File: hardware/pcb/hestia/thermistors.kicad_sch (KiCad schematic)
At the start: 60 parts, among them J10 Conn_01x02_Female, J11 Conn_01x02_Female, J12 Conn_01x02_Female, J13 Conn_01x02_Female, J14 Conn_01x02_Female, J15 Conn_01x02_Female, J16 Conn_01x02_Female, J7 Conn_01x02_Female, J8 Conn_01x02_Female, J9 Conn_01x02_Female, U4 MAX31725MTA+T, U5 MAX31725MTA+T, U6 MAX31725MTA+T, U7 MAX31725MTA+T

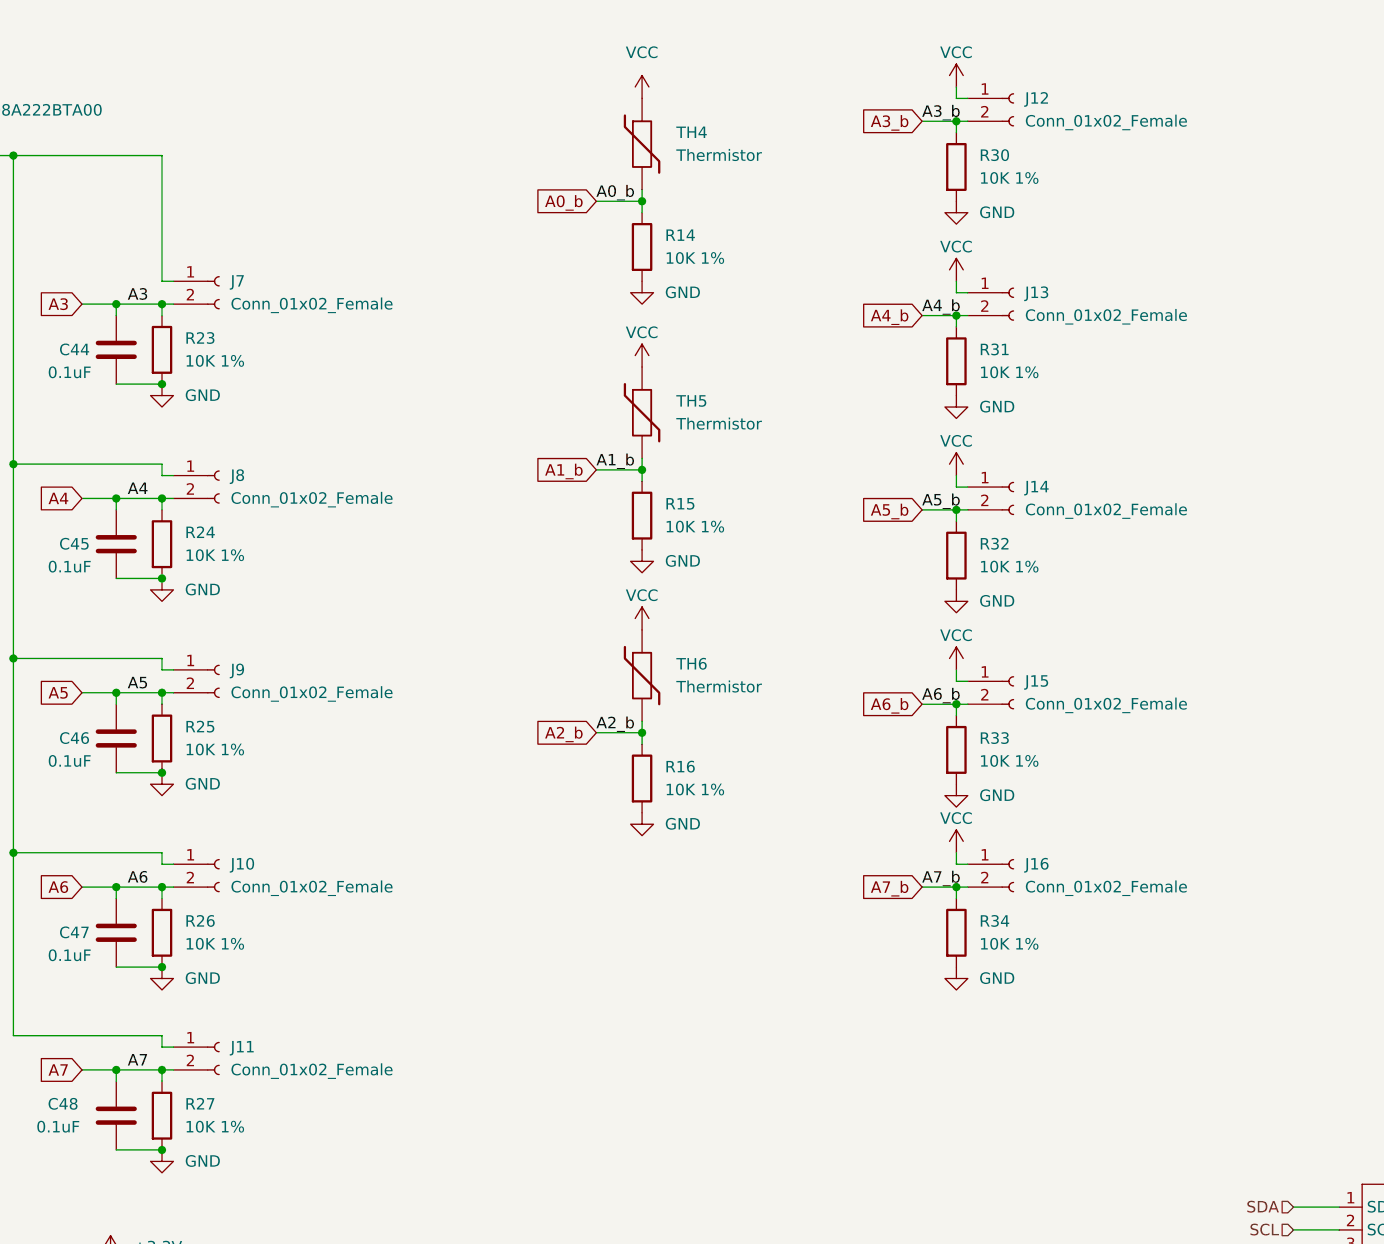
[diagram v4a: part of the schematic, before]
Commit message: don't update pcb from schematic yet. added and changed footprint info on schematic for 1.5mm pitch term pads, crystals, jtag vcc jumper. a bunch of components are out of sync with the pcb, the schematic is unaware that the components are already on the PCB. some components from the first versions were not in the hestia parts library - hopefully this commit adds them back? was a commit made without a pull?
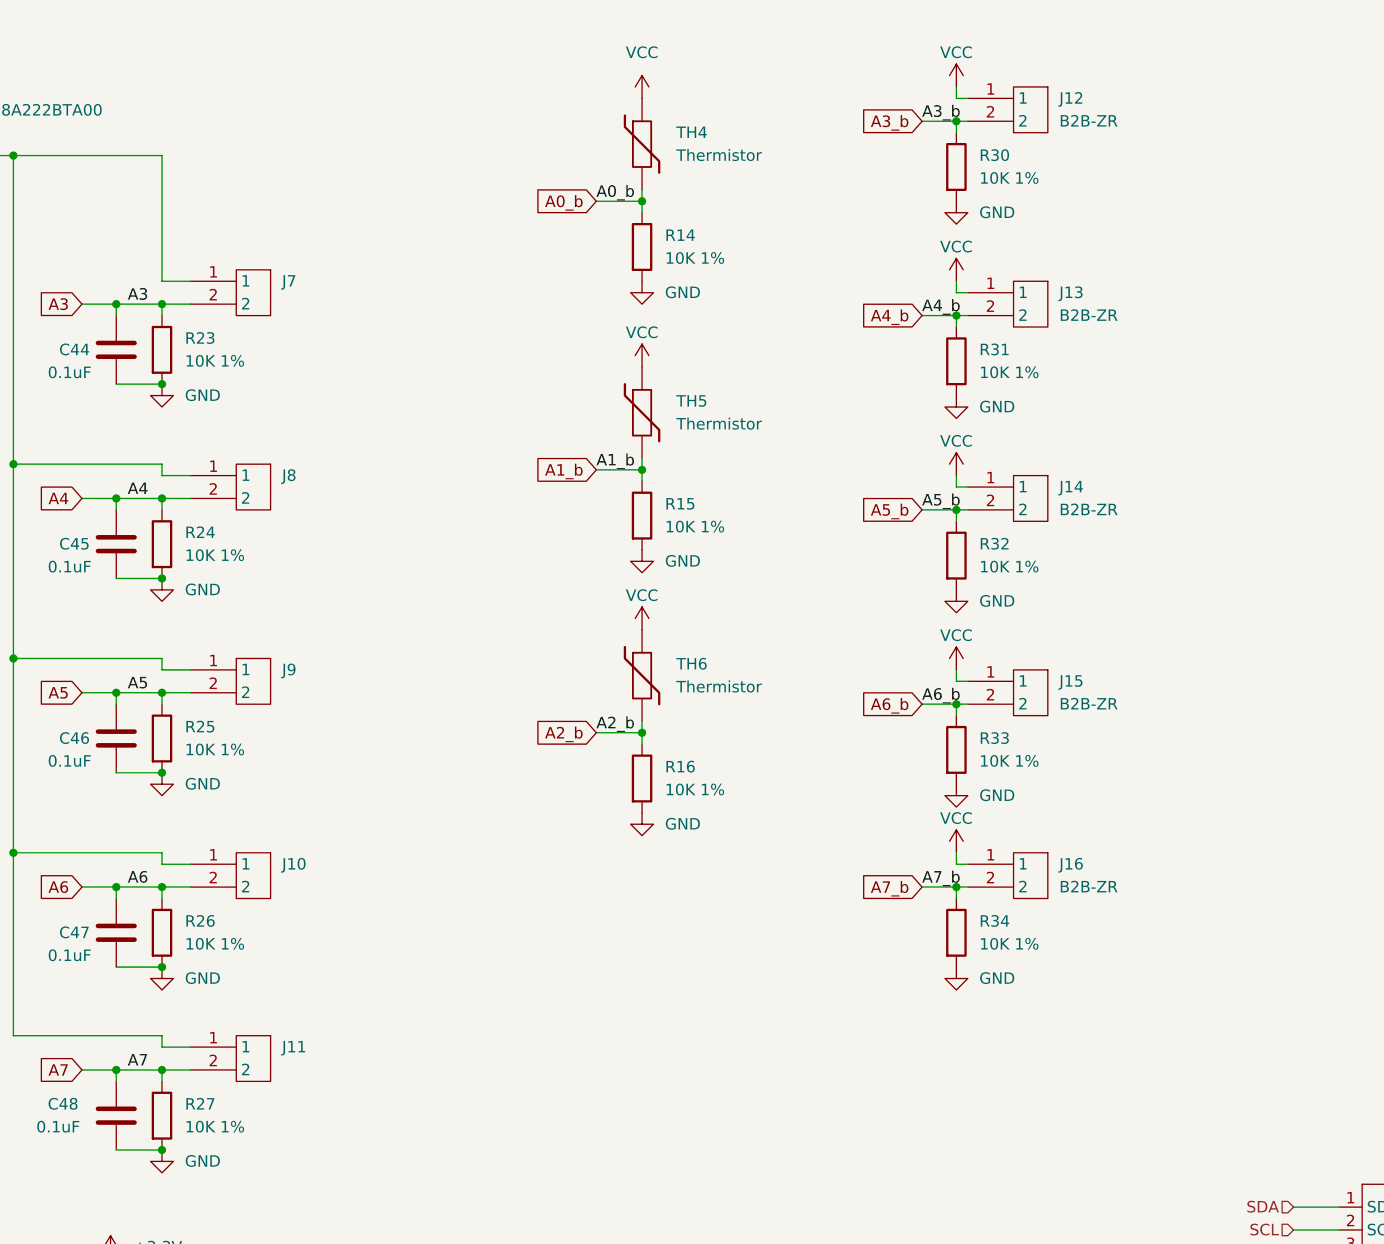
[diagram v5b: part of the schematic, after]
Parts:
- removed J10, J11, J12, J13, J14, J15, J16, J7, J8, J9: Conn_01x02_Female, Connector_PinHeader_1.27mm:PinHeader_1x02_P1.27mm_Vertical, symbol Connector:Conn_01x02_Female
- added J10, J11, J7, J8, J9: (no value), symbol Hestia:B2B-ZR
- added J12, J13, J14, J15, J16: B2B-ZR, Hestia:B2B-ZR(LF)(SN), symbol Hestia:B2B-ZR
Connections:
- net A3: now also J7.2
- net A3_b: now also J12.2
- net A4: now also J8.2
- net A4_b: now also J13.2
- net A5: now also J9.2
- net A5_b: now also J14.2
- net A6: now also J10.2
- net A6_b: now also J15.2
- net A7: now also J11.2
- net A7_b: now also J16.2
- net VCC: now also J12.1, J13.1, J14.1, J15.1, J16.1
- net at C50.1, FB4.1: now also J10.1, J11.1, J7.1, J8.1, J9.1

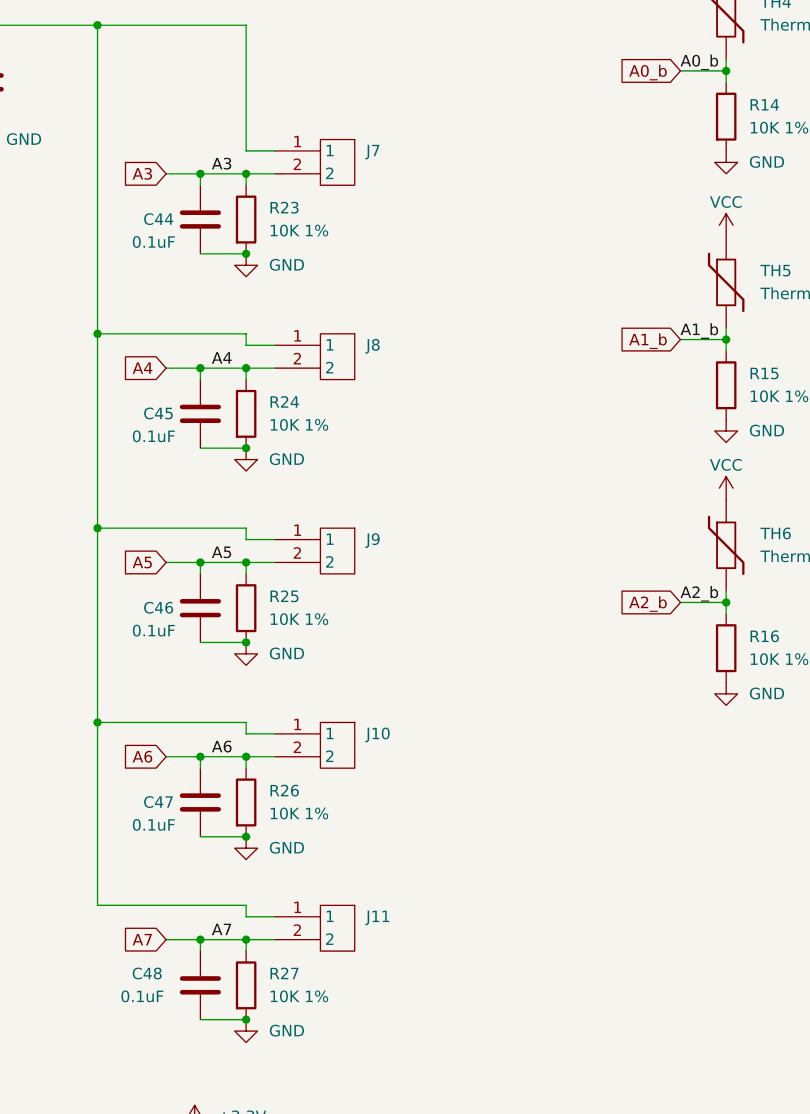
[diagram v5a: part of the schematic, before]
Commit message: Sorted out checmatic <=> pcb update sync. Changed JTAG pinheader to shrouded IDC connector footprint. temp place 2 pin 1.5mm pitch pin sockets. remove i2c voltage translator transistors, changed to i2c buffer ic. Added schematic symbol for cubesat board mount rods and linked to the hole footprint. TODO:rearrange components and traces, move J1&J2 by 3mm, wire restraint holes for wired thermistors, heater current measurement components, resettable fuses, bimetal switch footprint/pads, check I2C addresses
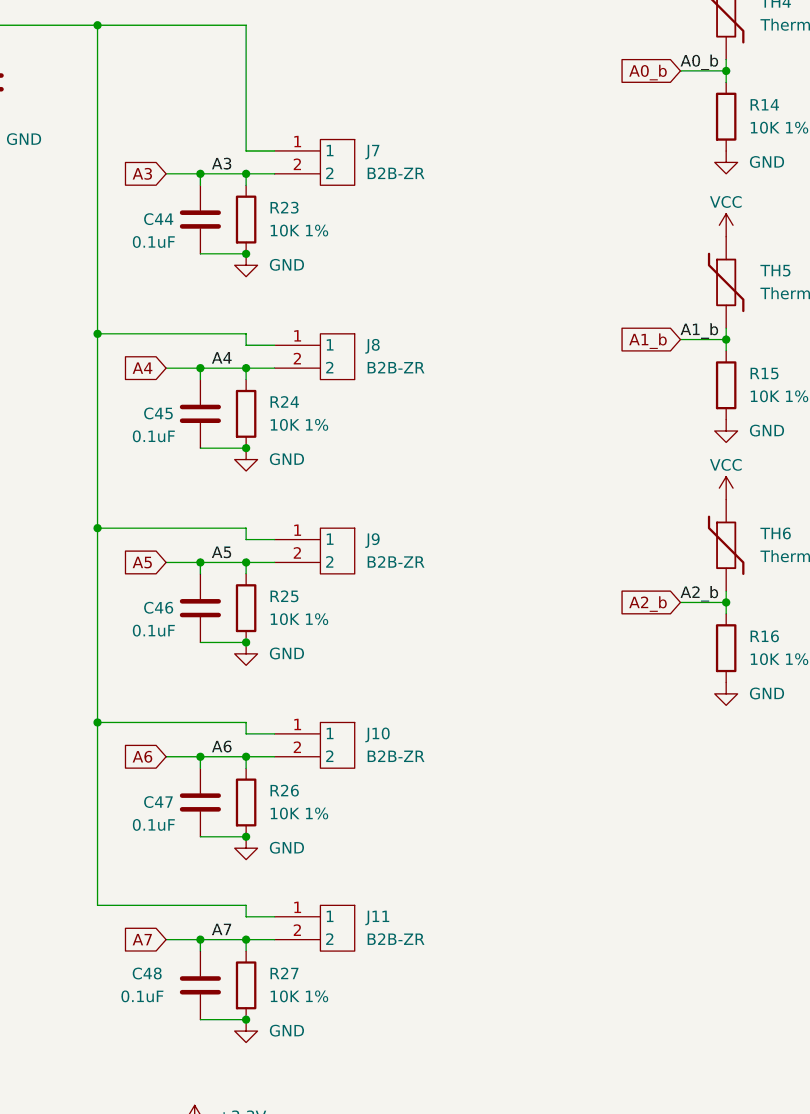
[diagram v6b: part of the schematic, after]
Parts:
- J10, J11, J7, J8, J9: value (none) -> B2B-ZR; footprint (none) -> Hestia:B2B-ZR(LF)(SN)
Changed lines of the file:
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@@
       (effects (font (size 1.27 1.27)) (justify right))
     )
-    (property "Value" "" (id 1) (at 109.22 67.3099 0)
-      (effects (font (size 1.27 1.27)) (justify right))
-    )
-    (property "Footprint" "" (id 2) (at 104.14 64.77 0)
+    (property "Value" "B2B-ZR" (id 1) (at 109.22 67.3099 0)
+      (effects (font (size 1.27 1.27)) (justify right))
+    )
+    (property "Footprint" "Hestia:B2B-ZR(LF)(SN)" (id 2) (at 104.14 64.77 0)
       (effects (font (size 1.27 1.27)) hide)
     )
@@
       (effects (font (size 1.27 1.27)) (justify right))
     )
-    (property "Value" "" (id 1) (at 109.22 45.7199 0)
-      (effects (font (size 1.27 1.27)) (justify right))
-    )
-    (property "Footprint" "" (id 2) (at 104.14 43.18 0)
+    (property "Value" "B2B-ZR" (id 1) (at 109.22 45.7199 0)
+      (effects (font (size 1.27 1.27)) (justify right))
+    )
+    (property "Footprint" "Hestia:B2B-ZR(LF)(SN)" (id 2) (at 104.14 43.18 0)
       (effects (font (size 1.27 1.27)) hide)
     )
@@
       (effects (font (size 1.27 1.27)) (justify right))
     )
-    (property "Value" "" (id 1) (at 109.22 88.8999 0)
-      (effects (font (size 1.27 1.27)) (justify right))
-    )
-    (property "Footprint" "" (id 2) (at 104.14 86.36 0)
+    (property "Value" "B2B-ZR" (id 1) (at 109.22 88.8999 0)
+      (effects (font (size 1.27 1.27)) (justify right))
+    )
+    (property "Footprint" "Hestia:B2B-ZR(LF)(SN)" (id 2) (at 104.14 86.36 0)
       (effects (font (size 1.27 1.27)) hide)
     )
@@
       (effects (font (size 1.27 1.27)) (justify right))
     )
-    (property "Value" "" (id 1) (at 109.22 110.4899 0)
-      (effects (font (size 1.27 1.27)) (justify right))
-    )
-    (property "Footprint" "" (id 2) (at 104.14 107.95 0)
+    (property "Value" "B2B-ZR" (id 1) (at 109.22 110.4899 0)
+      (effects (font (size 1.27 1.27)) (justify right))
+    )
+    (property "Footprint" "Hestia:B2B-ZR(LF)(SN)" (id 2) (at 104.14 107.95 0)
       (effects (font (size 1.27 1.27)) hide)
     )
@@
       (effects (font (size 1.27 1.27)) (justify right))
     )
-    (property "Value" "" (id 1) (at 109.22 130.8099 0)
-      (effects (font (size 1.27 1.27)) (justify right))
-    )
-    (property "Footprint" "" (id 2) (at 104.14 128.27 0)
-      (effects (font (size 1.27 1.27)) hide)
-    )
+    (property "Value" "B2B-ZR" (id 1) (at 109.22 130.8099 0)
+      (effects (font (size 1.27 1.27)) (justify right))
+    )
+    (property "Footprint" "Hestia:B2B-ZR(LF)(SN)" (id 2) (at 104.14 128.27 0)
+      (effects (font (size 1.27 1.27)) hide)
+    )

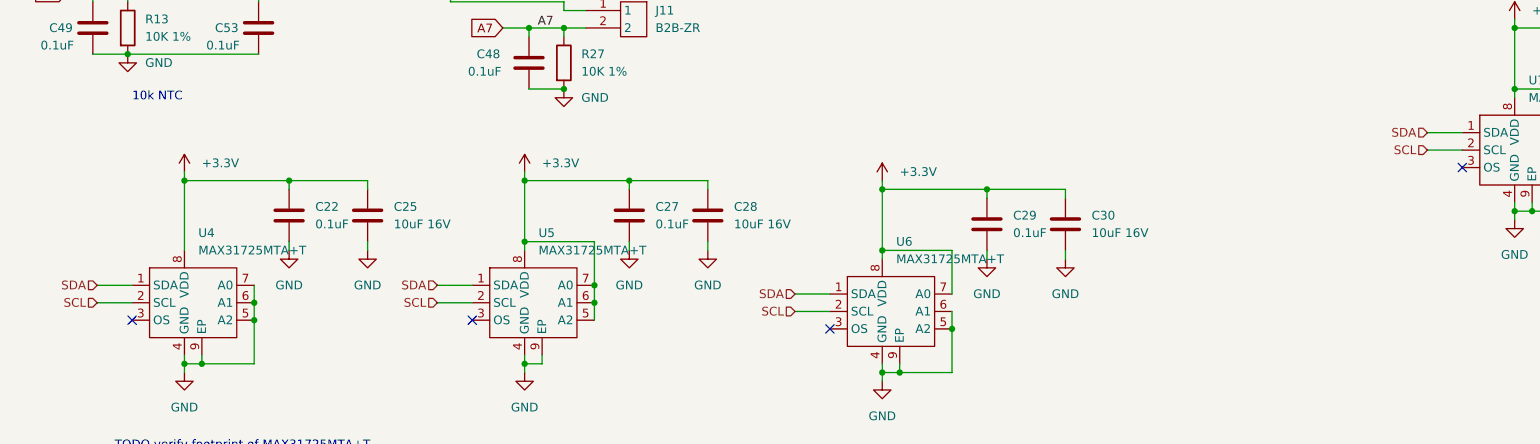
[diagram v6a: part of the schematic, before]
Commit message: more PCB trace changes on jtag, picolock connectors, i2c translator and I2C SDA,SCL, LEDs, Reset Switch
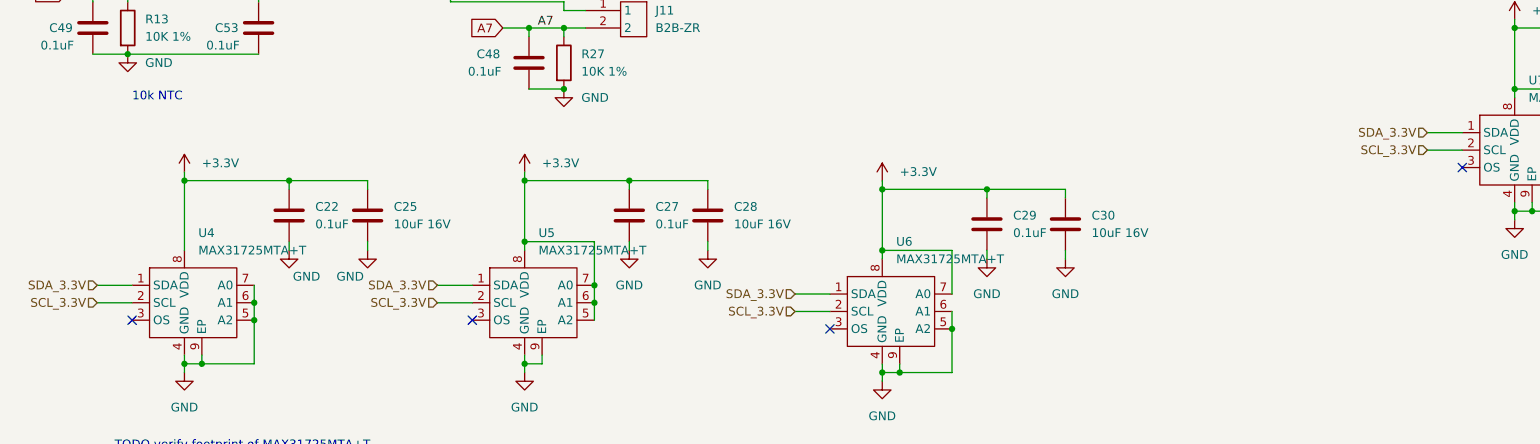
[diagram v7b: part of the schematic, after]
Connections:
- net SCL renamed SCL_3.3V
- net SDA renamed SDA_3.3V
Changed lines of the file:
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@@
     )
   )
-  (hierarchical_label "SDA" (shape input) (at 27.94 168.275 180)
-    (effects (font (size 1.27 1.27)) (justify right))
-  )
-  (hierarchical_label "SCL" (shape input) (at 221.615 148.59 180)
-    (effects (font (size 1.27 1.27)) (justify right))
-  )
-  (hierarchical_label "SDA" (shape input) (at 77.47 168.275 180)
-    (effects (font (size 1.27 1.27)) (justify right))
-  )
-  (hierarchical_label "SCL" (shape input) (at 27.94 170.815 180)
-    (effects (font (size 1.27 1.27)) (justify right))
-  )
-  (hierarchical_label "SCL" (shape input) (at 77.47 170.815 180)
-    (effects (font (size 1.27 1.27)) (justify right))
-  )
-  (hierarchical_label "SCL" (shape input) (at 129.54 172.085 180)
-    (effects (font (size 1.27 1.27)) (justify right))
-  )
-  (hierarchical_label "SDA" (shape input) (at 129.54 169.545 180)
-    (effects (font (size 1.27 1.27)) (justify right))
-  )
-  (hierarchical_label "SDA" (shape input) (at 221.615 146.05 180)
+  (hierarchical_label "SDA_3.3V" (shape input) (at 27.94 168.275 180)
+    (effects (font (size 1.27 1.27)) (justify right))
+  )
+  (hierarchical_label "SCL_3.3V" (shape input) (at 221.615 148.59 180)
+    (effects (font (size 1.27 1.27)) (justify right))
+  )
+  (hierarchical_label "SDA_3.3V" (shape input) (at 77.47 168.275 180)
+    (effects (font (size 1.27 1.27)) (justify right))
+  )
+  (hierarchical_label "SCL_3.3V" (shape input) (at 27.94 170.815 180)
+    (effects (font (size 1.27 1.27)) (justify right))
+  )
+  (hierarchical_label "SCL_3.3V" (shape input) (at 77.47 170.815 180)
+    (effects (font (size 1.27 1.27)) (justify right))
+  )
+  (hierarchical_label "SCL_3.3V" (shape input) (at 129.54 172.085 180)
+    (effects (font (size 1.27 1.27)) (justify right))
+  )
+  (hierarchical_label "SDA_3.3V" (shape input) (at 129.54 169.545 180)
+    (effects (font (size 1.27 1.27)) (justify right))
+  )
+  (hierarchical_label "SDA_3.3V" (shape input) (at 221.615 146.05 180)
     (effects (font (size 1.27 1.27)) (justify right))
   )
@@
   )
   (symbol (lib_id "power:GND") (at 67.31 163.195 0) (unit 1)
-    (in_bom yes) (on_board yes) (fields_autoplaced)
+    (in_bom yes) (on_board yes)
     (property "Reference" "#PWR0153" (id 0) (at 67.31 169.545 0)
       (effects (font (size 1.27 1.27)) hide)
     )
-    (property "Value" "GND" (id 1) (at 67.31 168.275 0))
+    (property "Value" "GND" (id 1) (at 64.77 167.005 0))
     (property "Footprint" "" (id 2) (at 67.31 163.195 0)
       (effects (font (size 1.27 1.27)) hide)
@@
   )
   (symbol (lib_id "power:GND") (at 55.88 163.195 0) (unit 1)
-    (in_bom yes) (on_board yes) (fields_autoplaced)
+    (in_bom yes) (on_board yes)
     (property "Reference" "#PWR0149" (id 0) (at 55.88 169.545 0)
       (effects (font (size 1.27 1.27)) hide)
     )
-    (property "Value" "GND" (id 1) (at 55.88 168.275 0))
+    (property "Value" "GND" (id 1) (at 58.42 167.005 0))
     (property "Footprint" "" (id 2) (at 55.88 163.195 0)
       (effects (font (size 1.27 1.27)) hide)
